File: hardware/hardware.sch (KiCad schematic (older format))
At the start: 8 parts

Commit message: Add custom symbols/footprints for teensy and audio board
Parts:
- removed J? (x4): Conn_01x14_Female, symbol Connector:Conn_01x14_Female
- added C?: 0.1uF, symbol Device:CP
- added D?: 1N4148, symbol Device:D
- added J?: Teensy3.2, symbol hardware:Teensy3.2
- added J?: TeensyAudioShield3.2, symbol hardware:TeensyAudioShield3.2
- added R?: 220, symbol Device:R
- added R?: 470, symbol Device:R
- added R? (x2): 47, symbol Device:R
- J?: Name (none) -> LCD
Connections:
- net labels added: +3.3V, +5V, A2, A3, A6, A7, BCLK, D2, D3, D4, D5, D8, DIN, DOUT, GND, GNDA, LRCLK, MCLK, MEMCS, MIDI_IN, MIDI_OUT, MISO, MOSI, SCK, SCL, SDA, SDCS, Vol
- wire segments 0 -> 82
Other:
- note removed: "LCD"
- note removed: "MIDI"
- note removed: "Teensy 3.2"
- note removed: "Teensy 3.2 AUdio PCB"
- moved on the sheet: J?, U?

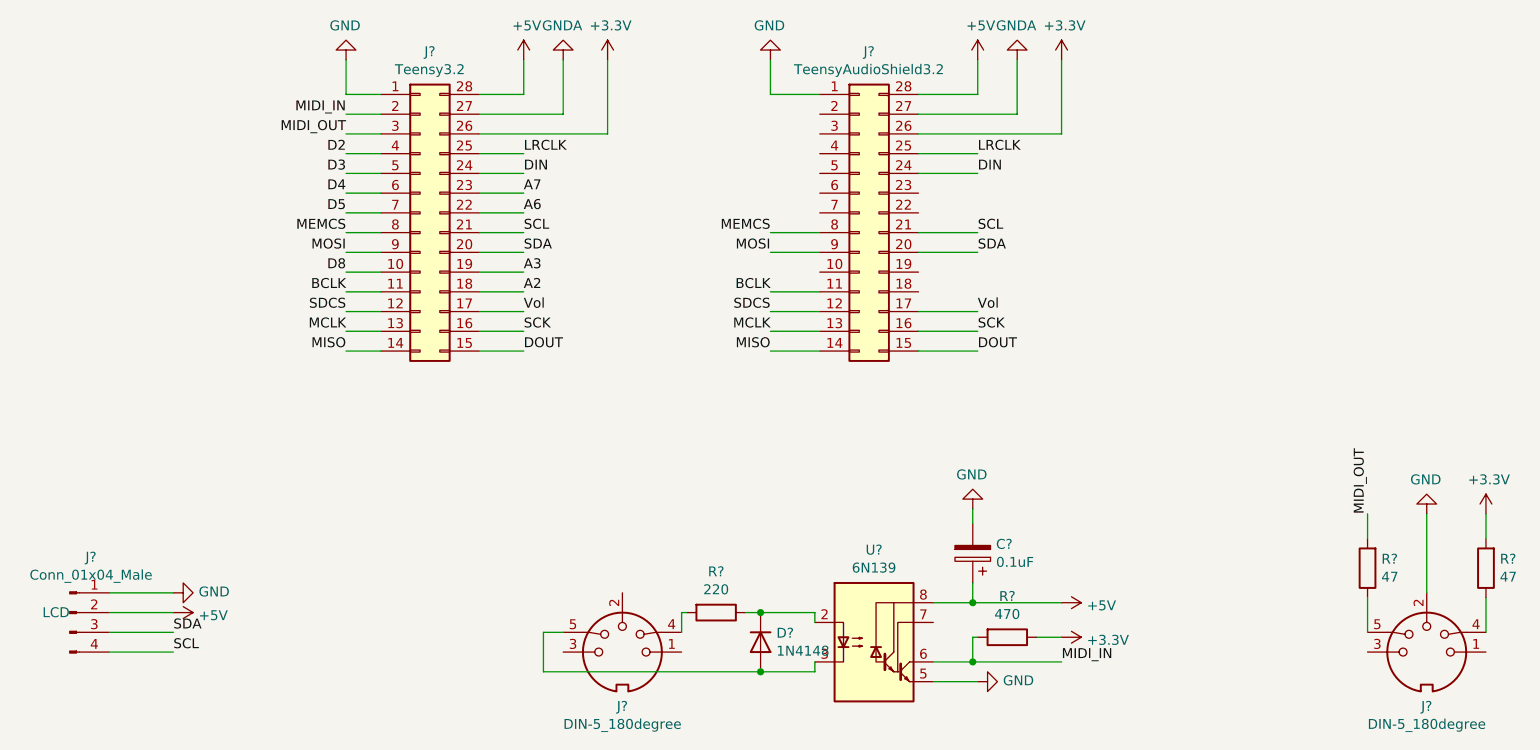
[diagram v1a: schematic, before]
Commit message: Add midi connector footprint
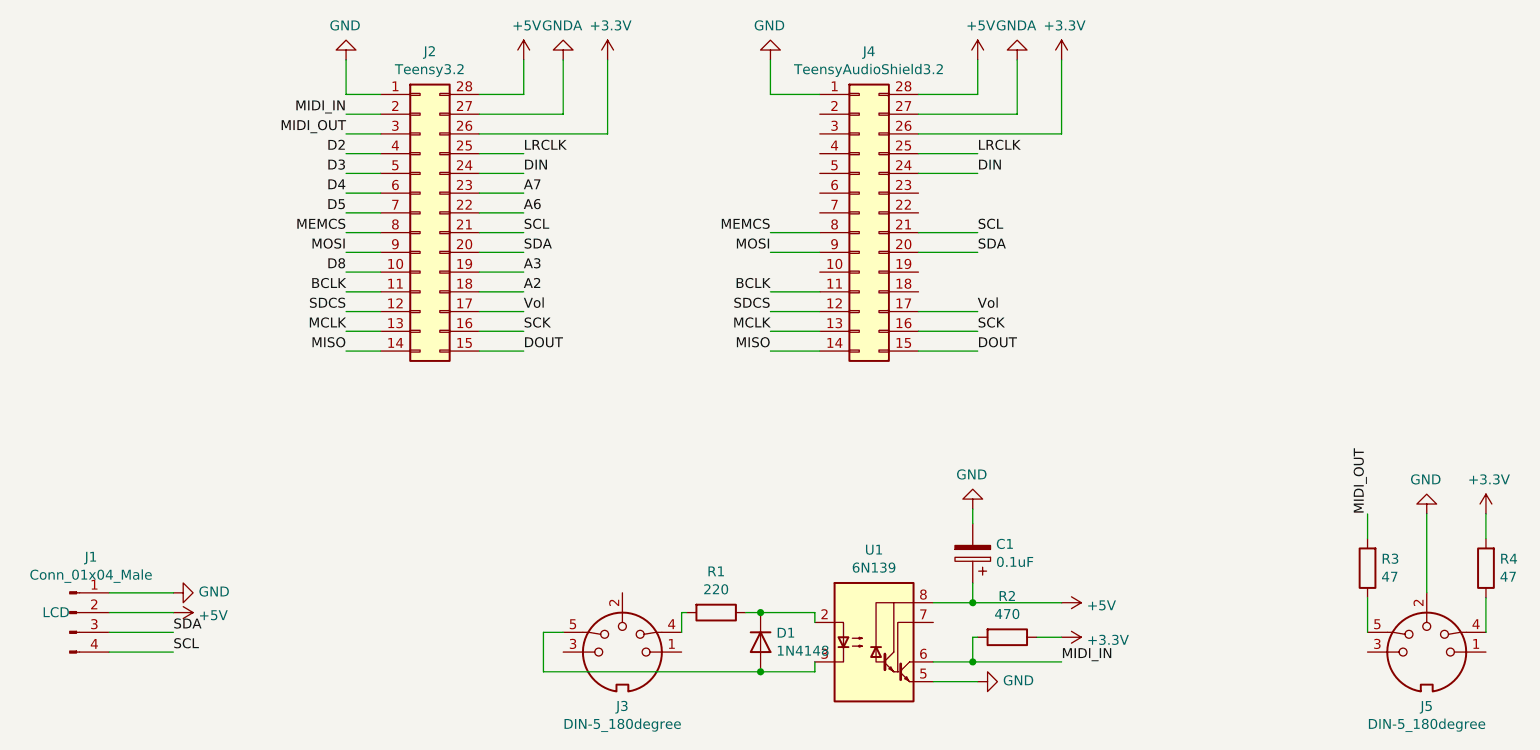
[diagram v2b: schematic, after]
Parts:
- C1: renamed from C?; footprint (none) -> Capacitor_THT:C_Rect_L7.0mm_W2.5mm_P5.00mm
- D1: renamed from D?; footprint (none) -> Diode_THT:D_DO-35_SOD27_P10.16mm_Horizontal
- J1: renamed from J?; footprint (none) -> Connector_PinHeader_2.54mm:PinHeader_1x04_P2.54mm_Vertical
- J2: renamed from J?; footprint (none) -> hardware:Teensy3.2
- J3, J5: renamed from J?; footprint (none) -> hardware:SDS-50J
- J4: renamed from J?; footprint (none) -> hardware:TeensyArduinoShield3.2
- R1, R2, R3, R4: renamed from R?; footprint (none) -> Resistor_THT:R_Axial_DIN0207_L6.3mm_D2.5mm_P10.16mm_Horizontal
- U1: renamed from U?; footprint (none) -> Package_DIP:DIP-8_W7.62mm_Socket_LongPads
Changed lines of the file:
@@
 $EndDescr
 $Comp
-L Connector:DIN-5_180degree J?
+L Connector:DIN-5_180degree J5
 U 1 1 5FB453D9
 P 8100 4250
-F 0 "J?" H 8100 3975 50  0000 C CNN
+F 0 "J5" H 8100 3975 50  0000 C CNN
 F 1 "DIN-5_180degree" H 8100 3884 50  0000 C CNN
-F 2 "" H 8100 4250 50  0001 C CNN
+F 2 "hardware:SDS-50J" H 8100 4250 50  0001 C CNN
 F 3 "http://www.mouser.com/ds/2/18/40_c091_abd_e-75918.pdf" H 8100 4250 50  0001 C CNN
 	1    8100 4250
@@
 $EndComp
 $Comp
-L Connector:DIN-5_180degree J?
+L Connector:DIN-5_180degree J3
 U 1 1 5FB4610C
 P 4025 4250
-F 0 "J?" H 4025 3975 50  0000 C CNN
+F 0 "J3" H 4025 3975 50  0000 C CNN
 F 1 "DIN-5_180degree" H 4025 3884 50  0000 C CNN
-F 2 "" H 4025 4250 50  0001 C CNN
+F 2 "hardware:SDS-50J" H 4025 4250 50  0001 C CNN
 F 3 "http://www.mouser.com/ds/2/18/40_c091_abd_e-75918.pdf" H 4025 4250 50  0001 C CNN
 	1    4025 4250
@@
 $EndComp
 $Comp
-L Connector:Conn_01x04_Male J?
+L Connector:Conn_01x04_Male J1
 U 1 1 5FB467C1
 P 1225 4050
-F 0 "J?" H 1333 4331 50  0000 C CNN
+F 0 "J1" H 1333 4331 50  0000 C CNN
 F 1 "Conn_01x04_Male" H 1333 4240 50  0000 C CNN
-F 2 "" H 1225 4050 50  0001 C CNN
+F 2 "Connector_PinHeader_2.54mm:PinHeader_1x04_P2.54mm_Vertical" H 1225 4050 50  0001 C CNN
 F 3 "~" H 1225 4050 50  0001 C CNN
 F 4 "LCD" H 1225 4050 50  0000 R CNN "Name"
@@
 $EndComp
 $Comp
-L Isolator:6N139 U?
+L Isolator:6N139 U1
 U 1 1 5FB479F7
 P 5300 4200
-F 0 "U?" H 5300 4667 50  0000 C CNN
+F 0 "U1" H 5300 4667 50  0000 C CNN
 F 1 "6N139" H 5300 4576 50  0000 C CNN
-F 2 "" H 5590 3900 50  0001 C CNN
+F 2 "Package_DIP:DIP-8_W7.62mm_Socket_LongPads" H 5590 3900 50  0001 C CNN
 F 3 "http://www.onsemi.com/pub/Collateral/HCPL2731-D.pdf" H 5590 3900 50  0001 C CNN
 	1    5300 4200
@@
 $EndComp
 $Comp
-L hardware:Teensy3.2 J?
+L hardware:Teensy3.2 J2
 U 1 1 5FB4EEE5
 P 3000 2025
-F 0 "J?" H 3050 2842 50  0000 C CNN
+F 0 "J2" H 3050 2842 50  0000 C CNN
 F 1 "Teensy3.2" H 3050 2751 50  0000 C CNN
-F 2 "" H 3000 2025 50  0001 C CNN
+F 2 "hardware:Teensy3.2" H 3000 2025 50  0001 C CNN
 F 3 "~" H 3000 2025 50  0001 C CNN
 	1    3000 2025
@@
 $EndComp
 $Comp
-L hardware:TeensyAudioShield3.2 J?
+L hardware:TeensyAudioShield3.2 J4
 U 1 1 5FB51D0C
 P 5225 2025
-F 0 "J?" H 5275 2842 50  0000 C CNN
+F 0 "J4" H 5275 2842 50  0000 C CNN
 F 1 "TeensyAudioShield3.2" H 5275 2751 50  0000 C CNN
-F 2 "" H 5225 2025 50  0001 C CNN
+F 2 "hardware:TeensyArduinoShield3.2" H 5225 2025 50  0001 C CNN
 F 3 "~" H 5225 2025 50  0001 C CNN
 	1    5225 2025
@@
 $EndComp
 $Comp
-L power:GND #PWR?
+L power:GND #PWR0101
 U 1 1 5FB63777
 P 2625 1250
-F 0 "#PWR?" H 2625 1000 50  0001 C CNN
+F 0 "#PWR0101" H 2625 1000 50  0001 C CNN
 F 1 "GND" H 2630 1077 50  0000 C CNN
 F 2 "" H 2625 1250 50  0001 C CNN
@@
 $EndComp
 $Comp
-L power:GND #PWR?
+L power:GND #PWR0102
 U 1 1 5FB6415E
 P 4775 1250
-F 0 "#PWR?" H 4775 1000 50  0001 C CNN
+F 0 "#PWR0102" H 4775 1000 50  0001 C CNN
 F 1 "GND" H 4780 1077 50  0000 C CNN
 F 2 "" H 4775 1250 50  0001 C CNN
@@
 	4775 1425 5025 1425
 $Comp
-L power:+5V #PWR?
+L power:+5V #PWR0103
 U 1 1 5FB64F21
 P 3525 1250
-F 0 "#PWR?" H 3525 1100 50  0001 C CNN
+F 0 "#PWR0103" H 3525 1100 50  0001 C CNN
 F 1 "+5V" H 3540 1423 50  0000 C CNN
 F 2 "" H 3525 1250 50  0001 C CNN
@@
 $EndComp
 $Comp
-L power:+5V #PWR?
+L power:+5V #PWR0104
 U 1 1 5FB65428
 P 5825 1250
-F 0 "#PWR?" H 5825 1100 50  0001 C CNN
+F 0 "#PWR0104" H 5825 1100 50  0001 C CNN
 F 1 "+5V" H 5840 1423 50  0000 C CNN
 F 2 "" H 5825 1250 50  0001 C CNN
@@
 	3525 1425 3525 1250
 $Comp
-L power:GNDA #PWR?
+L power:GNDA #PWR0105
 U 1 1 5FB660E2
 P 3725 1250
-F 0 "#PWR?" H 3725 1000 50  0001 C CNN
+F 0 "#PWR0105" H 3725 1000 50  0001 C CNN
 F 1 "GNDA" H 3730 1077 50  0000 C CNN
 F 2 "" H 3725 1250 50  0001 C CNN
@@
 $EndComp
 $Comp
-L power:GNDA #PWR?
+L power:GNDA #PWR0106
 U 1 1 5FB66E74
 P 6025 1250
-F 0 "#PWR?" H 6025 1000 50  0001 C CNN
+F 0 "#PWR0106" H 6025 1000 50  0001 C CNN
 F 1 "GNDA" H 6030 1077 50  0000 C CNN
 F 2 "" H 6025 1250 50  0001 C CNN
@@
 	6025 1525 6025 1250
 $Comp
-L power:+3.3V #PWR?
+L power:+3.3V #PWR0107
 U 1 1 5FB67F50
 P 3950 1250
-F 0 "#PWR?" H 3950 1100 50  0001 C CNN
+F 0 "#PWR0107" H 3950 1100 50  0001 C CNN
 F 1 "+3.3V" H 3965 1423 50  0000 C CNN
 F 2 "" H 3950 1250 50  0001 C CNN
@@
 $EndComp
 $Comp
-L power:+3.3V #PWR?
+L power:+3.3V #PWR0108
 U 1 1 5FB68784
 P 6250 1250
-F 0 "#PWR?" H 6250 1100 50  0001 C CNN
+F 0 "#PWR0108" H 6250 1100 50  0001 C CNN
 F 1 "+3.3V" H 6265 1423 50  0000 C CNN
 F 2 "" H 6250 1250 50  0001 C CNN
@@
 	5525 1725 5825 1725
 $Comp
-L power:GND #PWR?
+L power:GND #PWR0109
 U 1 1 5FB78D65
 P 1750 3950
-F 0 "#PWR?" H 1750 3700 50  0001 C CNN
+F 0 "#PWR0109" H 1750 3700 50  0001 C CNN
 F 1 "GND" V 1755 3822 50  0000 R CNN
 F 2 "" H 1750 3950 50  0001 C CNN
@@
 $EndComp
 $Comp
-L power:+5V #PWR?
+L power:+5V #PWR0110
 U 1 1 5FB79112
 P 1750 4050
-F 0 "#PWR?" H 1750 3900 50  0001 C CNN
+F 0 "#PWR0110" H 1750 3900 50  0001 C CNN
 F 1 "+5V" V 1765 4178 50  0000 L CNN
 F 2 "" H 1750 4050 50  0001 C CNN
@@
 	2625 1625 2800 1625
 $Comp
-L power:GND #PWR?
+L power:GND #PWR0111
 U 1 1 5FB808FE
 P 5825 4400
-F 0 "#PWR?" H 5825 4150 50  0001 C CNN
+F 0 "#PWR0111" H 5825 4150 50  0001 C CNN
 F 1 "GND" V 5830 4272 50  0000 R CNN
 F 2 "" H 5825 4400 50  0001 C CNN
@@
 	5600 4400 5825 4400
 $Comp
-L Device:D D?
+L Device:D D1
 U 1 1 5FB8347D
 P 4725 4200
-F 0 "D?" V 4679 4280 50  0000 L CNN
+F 0 "D1" V 4679 4280 50  0000 L CNN
 F 1 "1N4148" V 4770 4280 50  0000 L CNN
-F 2 "" H 4725 4200 50  0001 C CNN
+F 2 "Diode_THT:D_DO-35_SOD27_P10.16mm_Horizontal" H 4725 4200 50  0001 C CNN
 F 3 "~" H 4725 4200 50  0001 C CNN
 	1    4725 4200
@@
 $EndComp
 $Comp
-L Device:R R?
+L Device:R R1
 U 1 1 5FB83CFF
 P 4500 4050
-F 0 "R?" V 4293 4050 50  0000 C CNN
+F 0 "R1" V 4293 4050 50  0000 C CNN
 F 1 "220" V 4384 4050 50  0000 C CNN
-F 2 "" V 4430 4050 50  0001 C CNN
+F 2 "Resistor_THT:R_Axial_DIN0207_L6.3mm_D2.5mm_P10.16mm_Horizontal" V 4430 4050 50  0001 C CNN
 F 3 "~" H 4500 4050 50  0001 C CNN
 	1    4500 4050
@@
 	4325 4050 4325 4150
 $Comp
-L Device:R R?
+L Device:R R2
 U 1 1 5FB8CE40
 P 5975 4175
-F 0 "R?" V 5768 4175 50  0000 C CNN
+F 0 "R2" V 5768 4175 50  0000 C CNN
 F 1 "470" V 5859 4175 50  0000 C CNN
-F 2 "" V 5905 4175 50  0001 C CNN
+F 2 "Resistor_THT:R_Axial_DIN0207_L6.3mm_D2.5mm_P10.16mm_Horizontal" V 5905 4175 50  0001 C CNN
 F 3 "~" H 5975 4175 50  0001 C CNN
 	1    5975 4175
@@
 	5800 4175 5825 4175
 $Comp
-L power:+3.3V #PWR?
+L power:+3.3V #PWR0112
 U 1 1 5FB8EAF6
 P 6250 4175
-F 0 "#PWR?" H 6250 4025 50  0001 C CNN
+F 0 "#PWR0112" H 6250 4025 50  0001 C CNN
 F 1 "+3.3V" V 6265 4303 50  0000 L CNN
 F 2 "" H 6250 4175 50  0001 C CNN
@@
 Connection ~ 5800 4300
 $Comp
-L power:+5V #PWR?
+L power:+5V #PWR0113
 U 1 1 5FB92461
 P 6250 4000
-F 0 "#PWR?" H 6250 3850 50  0001 C CNN
+F 0 "#PWR0113" H 6250 3850 50  0001 C CNN
 F 1 "+5V" V 6265 4128 50  0000 L CNN
 F 2 "" H 6250 4000 50  0001 C CNN
@@
 	5600 4000 5800 4000
 $Comp
-L Device:CP C?
+L Device:CP C1
 U 1 1 5FB958A4
 P 5800 3750
-F 0 "C?" H 5682 3704 50  0000 R CNN
+F 0 "C1" H 5682 3704 50  0000 R CNN
 F 1 "0.1uF" H 5682 3795 50  0000 R CNN
-F 2 "" H 5838 3600 50  0001 C CNN
+F 2 "Capacitor_THT:C_Rect_L7.0mm_W2.5mm_P5.00mm" H 5838 3600 50  0001 C CNN
 F 3 "~" H 5800 3750 50  0001 C CNN
 	1    5800 3750
@@
 $EndComp
 $Comp
-L power:GND #PWR?
+L power:GND #PWR0114
 U 1 1 5FB96646
 P 5800 3525
-F 0 "#PWR?" H 5800 3275 50  0001 C CNN
+F 0 "#PWR0114" H 5800 3275 50  0001 C CNN
 F 1 "GND" H 5805 3352 50  0000 C CNN
 F 2 "" H 5800 3525 50  0001 C CNN
@@
 	5800 3600 5800 3525
 $Comp
-L power:GND #PWR?
+L power:GND #PWR0115
 U 1 1 5FB9ADFE
 P 8100 3550
-F 0 "#PWR?" H 8100 3300 50  0001 C CNN
+F 0 "#PWR0115" H 8100 3300 50  0001 C CNN
 F 1 "GND" H 8105 3377 50  0000 C CNN
 F 2 "" H 8100 3550 50  0001 C CNN
@@
 	8100 3550 8100 3950
 $Comp
-L power:+3.3V #PWR?
+L power:+3.3V #PWR0116
 U 1 1 5FB9E85A
 P 8400 3550
-F 0 "#PWR?" H 8400 3400 50  0001 C CNN
+F 0 "#PWR0116" H 8400 3400 50  0001 C CNN
 F 1 "+3.3V" H 8415 3723 50  0000 C CNN
 F 2 "" H 8400 3550 50  0001 C CNN
@@
 $EndComp
 $Comp
-L Device:R R?
+L Device:R R4
 U 1 1 5FB9EBAF
 P 8400 3825
-F 0 "R?" H 8330 3779 50  0000 R CNN
+F 0 "R4" H 8330 3779 50  0000 R CNN
 F 1 "47" H 8330 3870 50  0000 R CNN
-F 2 "" V 8330 3825 50  0001 C CNN
+F 2 "Resistor_THT:R_Axial_DIN0207_L6.3mm_D2.5mm_P10.16mm_Horizontal" V 8330 3825 50  0001 C CNN
 F 3 "~" H 8400 3825 50  0001 C CNN
 	1    8400 3825
@@
 MIDI_OUT
 $Comp
-L Device:R R?
+L Device:R R3
 U 1 1 5FBA2CF8
 P 7800 3825
-F 0 "R?" H 7730 3779 50  0000 R CNN
+F 0 "R3" H 7730 3779 50  0000 R CNN
 F 1 "47" H 7730 3870 50  0000 R CNN
-F 2 "" V 7730 3825 50  0001 C CNN
+F 2 "Resistor_THT:R_Axial_DIN0207_L6.3mm_D2.5mm_P10.16mm_Horizontal" V 7730 3825 50  0001 C CNN
 F 3 "~" H 7800 3825 50  0001 C CNN
 	1    7800 3825

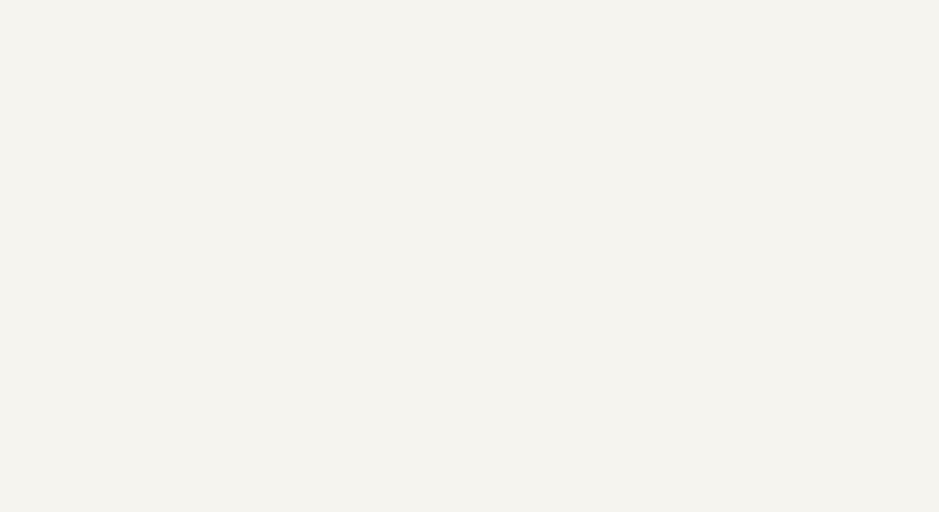
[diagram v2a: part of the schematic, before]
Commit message: Add some buttons and pots
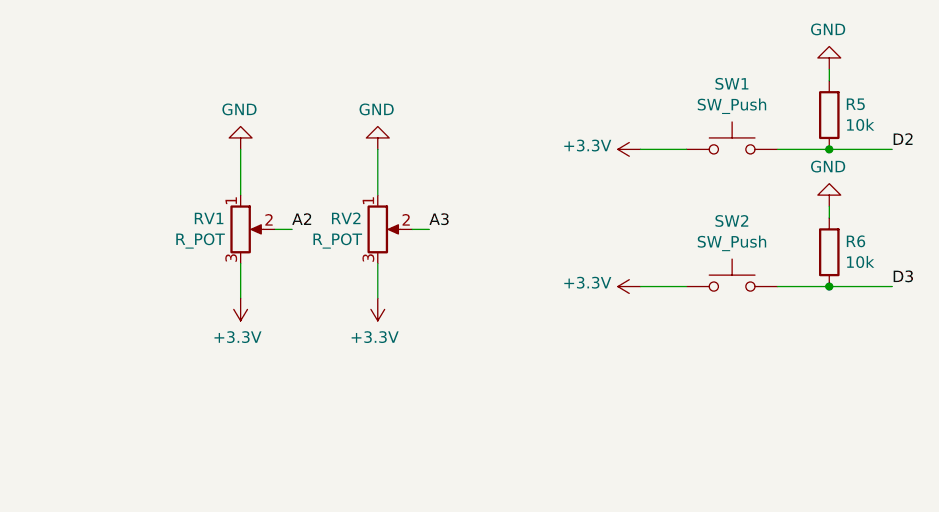
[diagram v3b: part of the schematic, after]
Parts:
- added R5, R6: 10k, Resistor_THT:R_Axial_DIN0207_L6.3mm_D2.5mm_P10.16mm_Horizontal, symbol Device:R
- added RV1, RV2: R_POT, Potentiometer_THT:Potentiometer_Alpha_RD901F-40-00D_Single_Vertical_CircularHoles, symbol Device:R_POT
- added SW1, SW2: SW_Push, Button_Switch_THT:SW_PUSH-12mm, symbol Switch:SW_Push
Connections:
- net +3V3: now also RV1.3, RV2.3, SW1.1, SW2.1
- net A2: now also RV1.2
- net A3: now also RV2.2
- net D2: now also R5.1, SW1.2
- net D3: now also R6.1, SW2.2
- net GND: now also R5.2, R6.2, RV1.1, RV2.1
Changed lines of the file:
@@
 Wire Wire Line
 	2800 2325 2625 2325
+$Comp
+L Device:R_POT RV1
+U 1 1 5FB51B6F
+P 7750 1900
+F 0 "RV1" H 7681 1946 50  0000 R CNN
+F 1 "R_POT" H 7681 1855 50  0000 R CNN
+F 2 "Potentiometer_THT:Potentiometer_Alpha_RD901F-40-00D_Single_Vertical_CircularHoles" H 7750 1900 50  0001 C CNN
+F 3 "~" H 7750 1900 50  0001 C CNN
+	1    7750 1900
+	1    0    0    -1
+$EndComp
+$Comp
+L Device:R_POT RV2
+U 1 1 5FB51FC5
+P 8350 1900
+F 0 "RV2" H 8281 1946 50  0000 R CNN
+F 1 "R_POT" H 8281 1855 50  0000 R CNN
+F 2 "Potentiometer_THT:Potentiometer_Alpha_RD901F-40-00D_Single_Vertical_CircularHoles" H 8350 1900 50  0001 C CNN
+F 3 "~" H 8350 1900 50  0001 C CNN
+	1    8350 1900
+	1    0    0    -1
+$EndComp
+$Comp
+L Switch:SW_Push SW1
+U 1 1 5FB524E6
+P 9900 1550
+F 0 "SW1" H 9900 1835 50  0000 C CNN
+F 1 "SW_Push" H 9900 1744 50  0000 C CNN
+F 2 "Button_Switch_THT:SW_PUSH-12mm" H 9900 1750 50  0001 C CNN
+F 3 "~" H 9900 1750 50  0001 C CNN
+	1    9900 1550
+	1    0    0    -1
+$EndComp
+$Comp
+L Switch:SW_Push SW2
+U 1 1 5FB52DA0
+P 9900 2150
+F 0 "SW2" H 9900 2435 50  0000 C CNN
+F 1 "SW_Push" H 9900 2344 50  0000 C CNN
+F 2 "Button_Switch_THT:SW_PUSH-12mm" H 9900 2350 50  0001 C CNN
+F 3 "~" H 9900 2350 50  0001 C CNN
+	1    9900 2150
+	1    0    0    -1
+$EndComp
+$Comp
+L Device:R R5
+U 1 1 5FB52F86
+P 10325 1400
+F 0 "R5" H 10255 1354 50  0000 R CNN
+F 1 "10k" H 10255 1445 50  0000 R CNN
+F 2 "Resistor_THT:R_Axial_DIN0207_L6.3mm_D2.5mm_P10.16mm_Horizontal" V 10255 1400 50  0001 C CNN
+F 3 "~" H 10325 1400 50  0001 C CNN
+	1    10325 1400
+	-1   0    0    1
+$EndComp
+$Comp
+L Device:R R6
+U 1 1 5FB55E00
+P 10325 2000
+F 0 "R6" H 10255 1954 50  0000 R CNN
+F 1 "10k" H 10255 2045 50  0000 R CNN
+F 2 "Resistor_THT:R_Axial_DIN0207_L6.3mm_D2.5mm_P10.16mm_Horizontal" V 10255 2000 50  0001 C CNN
+F 3 "~" H 10325 2000 50  0001 C CNN
+	1    10325 2000
+	-1   0    0    1
+$EndComp
+Text Label 10600 1550 0    50   ~ 0
+D2
+Text Label 10600 2150 0    50   ~ 0
+D3
+$Comp
+L power:+3.3V #PWR0117
+U 1 1 5FB56925
+P 9500 1550
+F 0 "#PWR0117" H 9500 1400 50  0001 C CNN
+F 1 "+3.3V" V 9515 1678 50  0000 L CNN
+F 2 "" H 9500 1550 50  0001 C CNN
+F 3 "" H 9500 1550 50  0001 C CNN
+	1    9500 1550
+	0    -1   -1   0
+$EndComp
+$Comp
+L power:+3.3V #PWR0118
+U 1 1 5FB56D78
+P 9500 2150
+F 0 "#PWR0118" H 9500 2000 50  0001 C CNN
+F 1 "+3.3V" V 9515 2278 50  0000 L CNN
+F 2 "" H 9500 2150 50  0001 C CNN
+F 3 "" H 9500 2150 50  0001 C CNN
+	1    9500 2150
+	0    -1   -1   0
+$EndComp
+$Comp
+L power:GND #PWR0119
+U 1 1 5FB5718C
+P 10325 1200
+F 0 "#PWR0119" H 10325 950 50  0001 C CNN
+F 1 "GND" H 10330 1027 50  0000 C CNN
+F 2 "" H 10325 1200 50  0001 C CNN
+F 3 "" H 10325 1200 50  0001 C CNN
+	1    10325 1200
+	-1   0    0    1
+$EndComp
+$Comp
+L power:GND #PWR0120
+U 1 1 5FB5776F
+P 10325 1800
+F 0 "#PWR0120" H 10325 1550 50  0001 C CNN
+F 1 "GND" H 10330 1627 50  0000 C CNN
+F 2 "" H 10325 1800 50  0001 C CNN
+F 3 "" H 10325 1800 50  0001 C CNN
+	1    10325 1800
+	-1   0    0    1
+$EndComp
+Wire Wire Line
+	9500 1550 9700 1550
+Wire Wire Line
+	10100 1550 10325 1550
+Wire Wire Line
+	10600 1550 10325 1550
+Connection ~ 10325 1550
+Wire Wire Line
+	10325 1200 10325 1250
+Wire Wire Line
+	10325 1800 10325 1850
+Wire Wire Line
+	9500 2150 9700 2150
+Wire Wire Line
+	10100 2150 10325 2150
+Wire Wire Line
+	10600 2150 10325 2150
+Connection ~ 10325 2150
+$Comp
+L power:+3.3V #PWR0121
+U 1 1 5FB6CE55
+P 7750 2200
+F 0 "#PWR0121" H 7750 2050 50  0001 C CNN
+F 1 "+3.3V" H 7765 2373 50  0000 C CNN
+F 2 "" H 7750 2200 50  0001 C CNN
+F 3 "" H 7750 2200 50  0001 C CNN
+	1    7750 2200
+	-1   0    0    1
+$EndComp
+$Comp
+L power:+3.3V #PWR0122
+U 1 1 5FB6D865
+P 8350 2200
+F 0 "#PWR0122" H 8350 2050 50  0001 C CNN
+F 1 "+3.3V" H 8365 2373 50  0000 C CNN
+F 2 "" H 8350 2200 50  0001 C CNN
+F 3 "" H 8350 2200 50  0001 C CNN
+	1    8350 2200
+	-1   0    0    1
+$EndComp
+$Comp
+L power:GND #PWR0123
+U 1 1 5FB6DAFA
+P 7750 1550
+F 0 "#PWR0123" H 7750 1300 50  0001 C CNN
+F 1 "GND" H 7755 1377 50  0000 C CNN
+F 2 "" H 7750 1550 50  0001 C CNN
+F 3 "" H 7750 1550 50  0001 C CNN
+	1    7750 1550
+	-1   0    0    1
+$EndComp
+$Comp
+L power:GND #PWR0124
+U 1 1 5FB6DE82
+P 8350 1550
+F 0 "#PWR0124" H 8350 1300 50  0001 C CNN
+F 1 "GND" H 8355 1377 50  0000 C CNN
+F 2 "" H 8350 1550 50  0001 C CNN
+F 3 "" H 8350 1550 50  0001 C CNN
+	1    8350 1550
+	-1   0    0    1
+$EndComp
+Text Label 7975 1900 0    50   ~ 0
+A2
+Text Label 8575 1900 0    50   ~ 0
+A3
+Wire Wire Line
+	7900 1900 7975 1900
+Wire Wire Line
+	7750 1550 7750 1750
+Wire Wire Line
+	7750 2200 7750 2050
+Wire Wire Line
+	8350 2200 8350 2050
+Wire Wire Line
+	8350 1750 8350 1550
+Wire Wire Line
+	8575 1900 8500 1900
 $EndSCHEMATC
